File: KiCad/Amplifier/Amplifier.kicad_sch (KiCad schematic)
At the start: 12 parts, among them Q5 NPN, Q6 NPN, U6 TL074

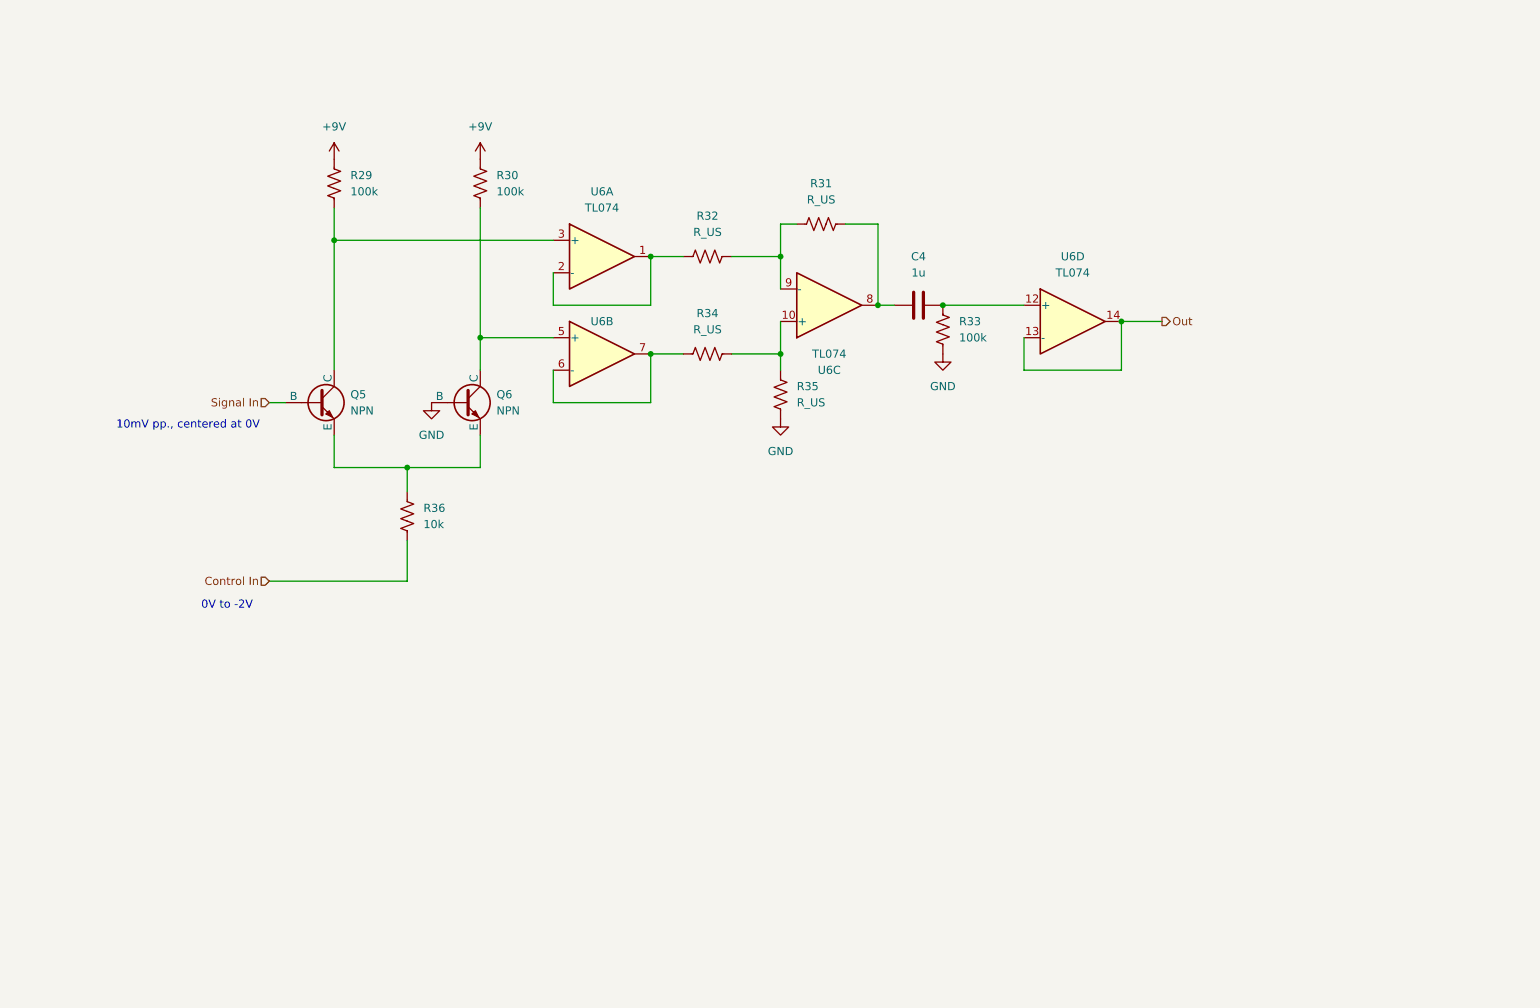
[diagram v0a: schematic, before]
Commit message: started separating into different boards, partially fixed envelope generator
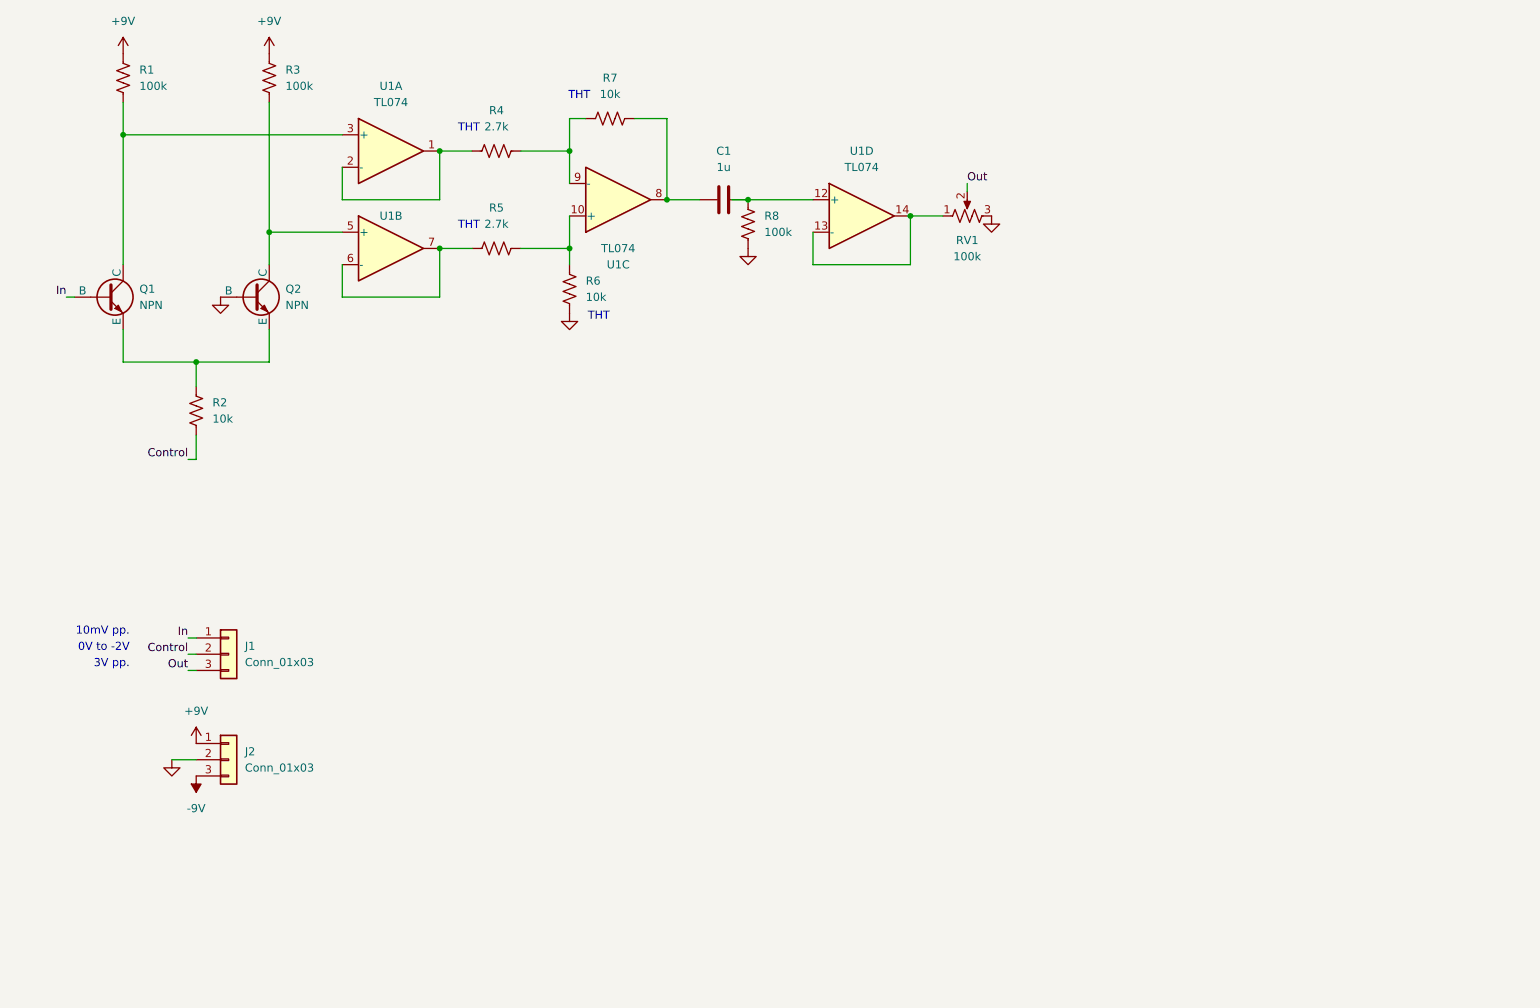
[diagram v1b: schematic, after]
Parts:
- added J1, J2: Conn_01x03, symbol Connector_Generic:Conn_01x03
- added RV1: 100k, symbol Device:R_Potentiometer_US
- R4: renamed from R32; value R_US -> 2.7k
- R5: renamed from R34; value R_US -> 2.7k
- R6: renamed from R35; value R_US -> 10k
- R7: renamed from R31; value R_US -> 10k
- renumbered C4 to C1, Q5 to Q1, Q6 to Q2, R29 to R1, R36 to R2, R30 to R3, R33 to R8, U6 to U1
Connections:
- net +9V: now also J2.1 (Pin_1)
- net GND: now also J2.2 (Pin_2), RV1.3
- net Out: now also J1.3 (Pin_3), RV1.2; no longer U1.13 (-), U1.14
- net Control In renamed Control
- net Control: now also J1.2 (Pin_2)
- net Signal In renamed In
- net In: now also J1.1 (Pin_1)
- new net: RV1.1, U1.13 (-), U1.14
- new net -9V: J2.3 (Pin_3)
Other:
- note added: "10mV pp."
- note added: "3V pp."
- note added: "THT"
- note removed: "10mV pp., centered at 0V"
- moved on the sheet: C1, Q1, Q2, R1, R2, R3, R4, R5, R6, R7, R8, U1A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

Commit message: fixed power board, replaced sketchy voltage divider - op amp cct. with an LDO to product +5V
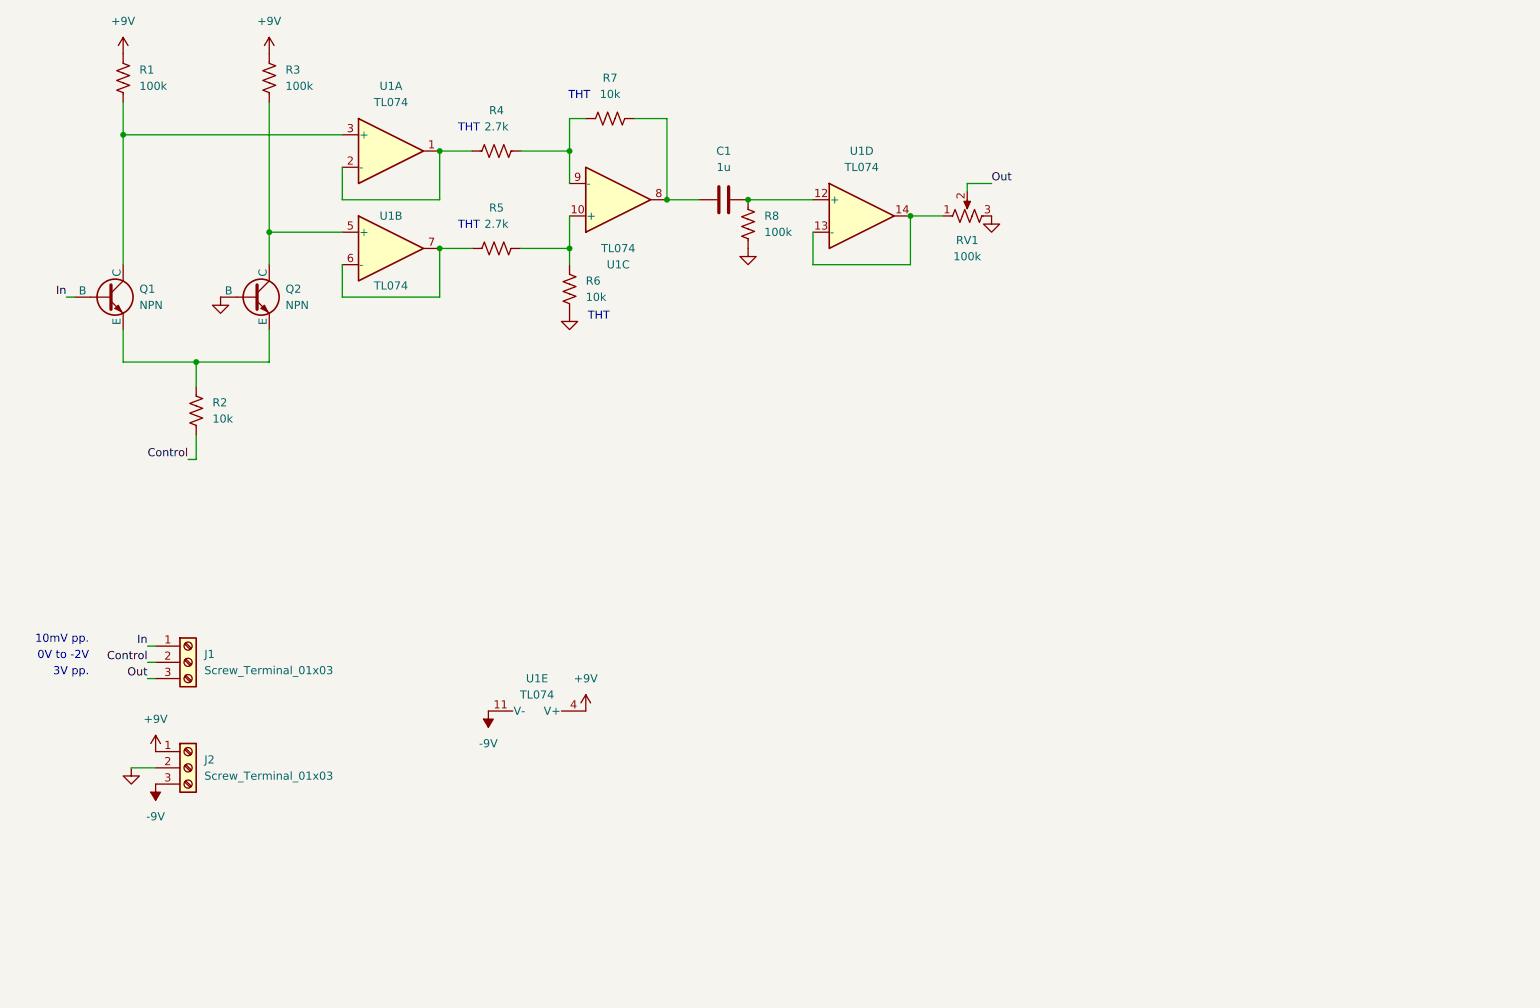
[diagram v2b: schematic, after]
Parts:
- removed J1, J2: Conn_01x03, symbol Connector_Generic:Conn_01x03
- added J1, J2: Screw_Terminal_01x03, symbol Connector:Screw_Terminal_01x03
- added unit 5 of U1
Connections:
- net +9V: now also J2.1 (Pin_1), U1.4 (V+)
- net -9V: now also J2.3 (Pin_3), U1.11 (V-)
- net Control: now also J1.2 (Pin_2)
- net GND: now also J2.2 (Pin_2)
- net In: now also J1.1 (Pin_1)
- net Out: now also J1.3 (Pin_3)

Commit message: finished separating into separate kicad projects
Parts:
- added C? (x2): 0.1u, symbol Device:C_Small
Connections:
- net +9V: now also C?.2
- net -9V: now also C?.1
- net GND: now also C?.1, C?.2
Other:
- moved on the sheet: U1E

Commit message: made oscillator more adjustable
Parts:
- gave numbers to parts that had none: 2
- renumbered C1 to C2
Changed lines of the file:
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@@
 		(dnp no)
 		(fields_autoplaced yes)
-		(property "Reference" "#PWR011"
+		(property "Reference" "#PWR08"
 			(at 99.06 129.54 0)
 			(hide yes)
@@
 			(project "Amplifier"
 				(path "/4b9119d6-fa5d-4921-8a56-e3e986a94725"
-					(reference "#PWR011")
+					(reference "#PWR08")
 					(unit 1)
 				)
@@
 		(dnp no)
 		(fields_autoplaced yes)
-		(property "Reference" "#PWR09"
+		(property "Reference" "#PWR013"
 			(at 166.37 60.96 0)
 			(hide yes)
@@
 			(project "Amplifier"
 				(path "/4b9119d6-fa5d-4921-8a56-e3e986a94725"
-					(reference "#PWR09")
+					(reference "#PWR013")
 					(unit 1)
 				)
@@
 		(dnp no)
 		(fields_autoplaced yes)
-		(property "Reference" "#PWR08"
+		(property "Reference" "#PWR011"
 			(at 128.27 66.04 0)
 			(hide yes)
@@
 			(project "Amplifier"
 				(path "/4b9119d6-fa5d-4921-8a56-e3e986a94725"
-					(reference "#PWR08")
+					(reference "#PWR011")
 					(unit 1)
 				)
@@
 		(dnp no)
 		(fields_autoplaced yes)
-		(property "Reference" "C1"
+		(property "Reference" "C2"
 			(at 124.46 44.45 90)
 			(show_name no)
@@
 			(project "Amplifier"
 				(path "/4b9119d6-fa5d-4921-8a56-e3e986a94725"
-					(reference "C1")
+					(reference "C2")
 					(unit 1)
 				)
@@
 		(dnp no)
 		(fields_autoplaced yes)
-		(property "Reference" "#PWR013"
+		(property "Reference" "#PWR012"
 			(at 129.54 139.7 0)
 			(hide yes)
@@
 			(project "Amplifier"
 				(path "/4b9119d6-fa5d-4921-8a56-e3e986a94725"
-					(reference "#PWR013")
+					(reference "#PWR012")
 					(unit 1)
 				)
@@
 		(dnp no)
 		(fields_autoplaced yes)
-		(property "Reference" "#PWR07"
+		(property "Reference" "#PWR09"
 			(at 100.33 76.2 0)
 			(hide yes)
@@
 			(project "Amplifier"
 				(path "/4b9119d6-fa5d-4921-8a56-e3e986a94725"
-					(reference "#PWR07")
+					(reference "#PWR09")
 					(unit 1)
 				)
@@
 		(dnp no)
 		(fields_autoplaced yes)
-		(property "Reference" "#PWR012"
+		(property "Reference" "#PWR07"
 			(at 88.9 139.7 0)
 			(hide yes)
@@
 			(project "Amplifier"
 				(path "/4b9119d6-fa5d-4921-8a56-e3e986a94725"
-					(reference "#PWR012")
+					(reference "#PWR07")
 					(unit 1)
 				)
@@
 		(dnp no)
 		(fields_autoplaced yes)
-		(property "Reference" "C?"
+		(property "Reference" "C3"
 			(at 124.4536 127 90)
 			(show_name no)
@@
 			(project "Amplifier"
 				(path "/4b9119d6-fa5d-4921-8a56-e3e986a94725"
-					(reference "C?")
+					(reference "C3")
 					(unit 1)
 				)
@@
 		(dnp no)
 		(fields_autoplaced yes)
-		(property "Reference" "C?"
+		(property "Reference" "C1"
 			(at 93.9736 127 90)
 			(show_name no)
@@
 			(project "Amplifier"
 				(path "/4b9119d6-fa5d-4921-8a56-e3e986a94725"
-					(reference "C?")
-					(unit 1)
-				)
+					(reference "C1")
+					(unit 1)
+				)

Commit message: added test points
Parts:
- added TP? (x4): TestPoint_Small, symbol Connector:TestPoint_Small
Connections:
- net Control: now also TP?.1
- net GND: now also TP?.1
- net In: now also TP?.1
- net Out: now also TP?.1

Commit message: added power indicator LEDs
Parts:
- added D1, D2: LED, symbol Device:LED
- added R7, R8: R_US, symbol Device:R_US
- gave numbers to parts that had none: 4
- renumbered R8 to R10, R7 to R9
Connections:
- net +9V: now also D1.2 (A)
- net -9V: now also R8.2
- net GND: now also D2.2 (A), R7.2
- new net: D1.1 (K), R7.1
- new net: D2.1 (K), R8.1

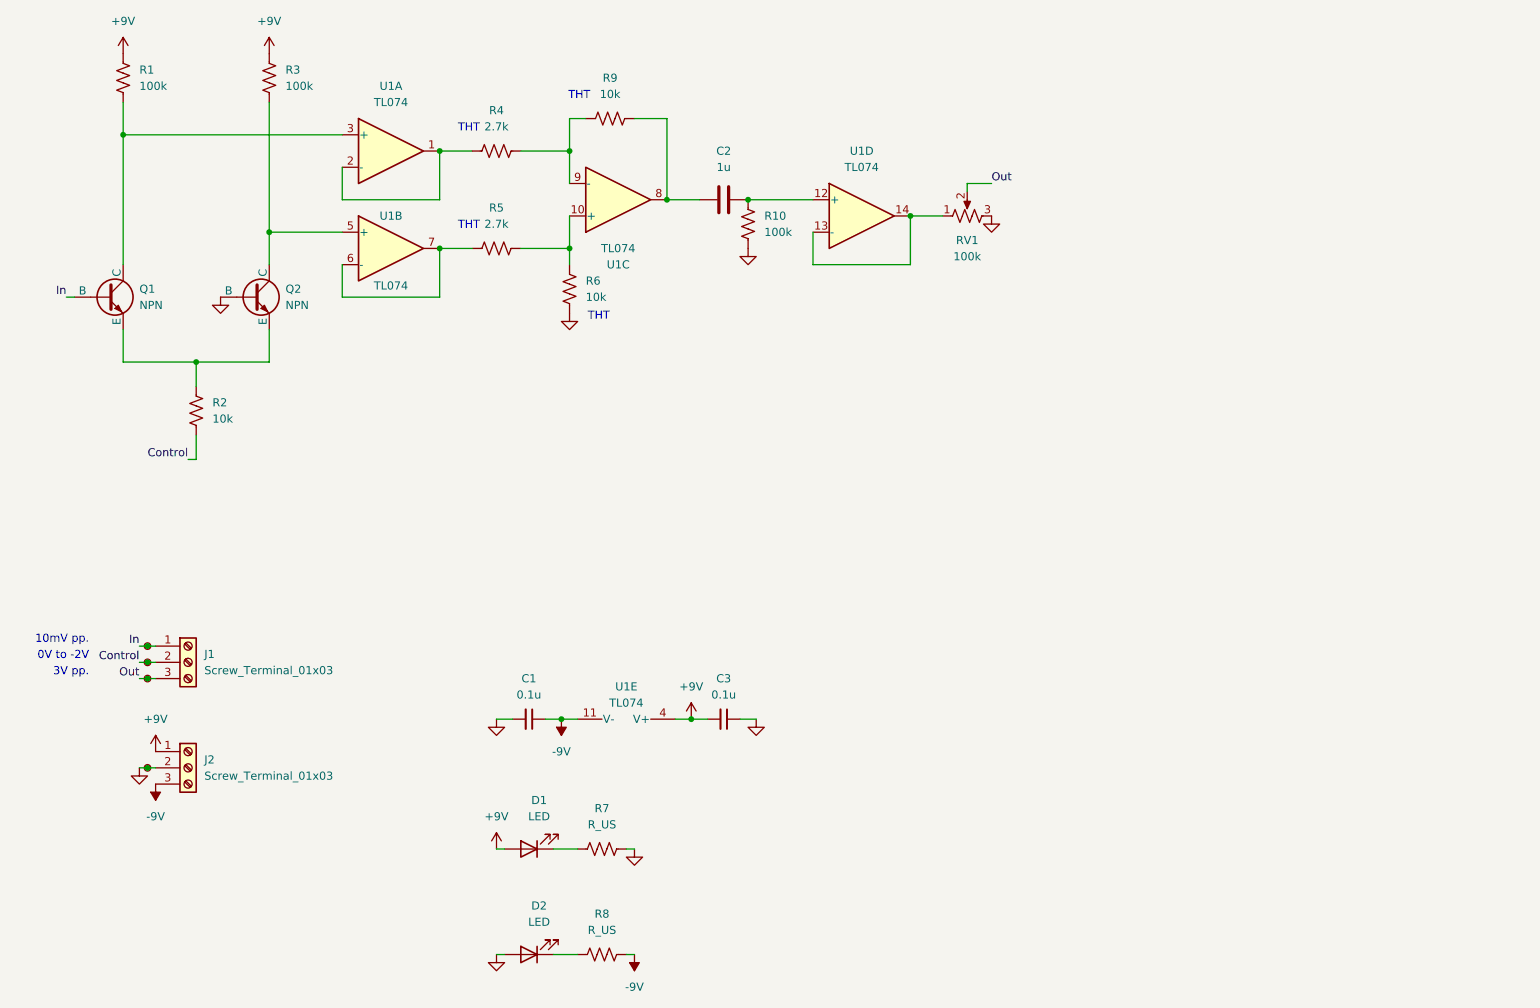
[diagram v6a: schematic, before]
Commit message: amplifier pcb layout done
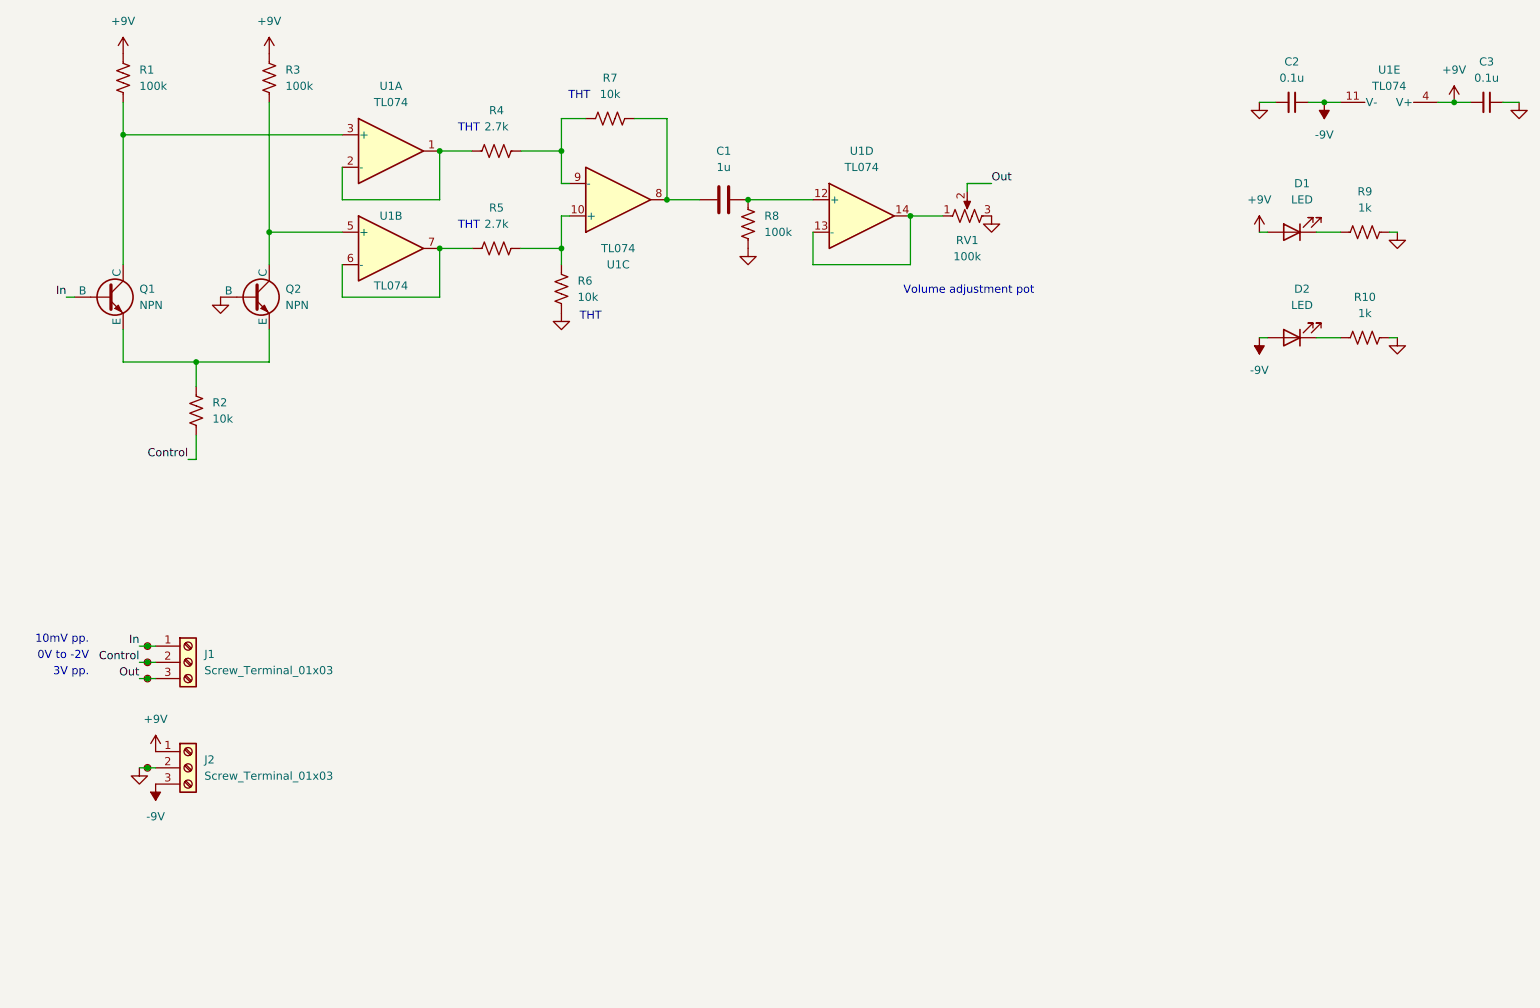
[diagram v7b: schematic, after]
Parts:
- C2: renamed from C1; footprint (none) -> Capacitor_SMD:C_0805_2012Metric
- C3: footprint (none) -> Capacitor_SMD:C_0805_2012Metric
- D1, D2: footprint (none) -> LED_THT:LED_D5.0mm
- J1, J2: footprint (none) -> Header 691137710003:691137710003
- R1, R2, R3: footprint Resistor_SMD:R_0603_1608Metric -> Resistor_SMD:R_0805_2012Metric
- R10: renamed from R8; value R_US -> 1k; footprint (none) -> Resistor_THT:R_Axial_DIN0207_L6.3mm_D2.5mm_P7.62mm_Horizontal
- R8: renamed from R10; footprint Resistor_SMD:R_0603_1608Metric -> Resistor_SMD:R_0805_2012Metric
- R9: renamed from R7; value R_US -> 1k; footprint (none) -> Resistor_THT:R_Axial_DIN0207_L6.3mm_D2.5mm_P7.62mm_Horizontal
- RV1: footprint (none) -> Potentiometer_THT:Potentiometer_Bourns_PTV09A-2_Single_Horizontal
- TP1, TP2, TP3, TP4: footprint (none) -> TestPoint:TestPoint_Keystone_5000-5004_Miniature
- U1: footprint (none) -> Package_DIP:DIP-14_W7.62mm
- renumbered C2 to C1, R9 to R7
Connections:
- net -9V: now also D2.2 (A); no longer R10.2
- net GND: now also R10.2; no longer D2.2 (A)
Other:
- note added: "Volume adjustment pot"
- moved on the sheet: C2, C3, D1, D2, R10, R6, R9, U1E

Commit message: removed unnecessary buffer before filter's output
this drops the number of op amps from 5 to 4, allowing us to use 1 IC instead of 2 ICs with 3 unused circuits.
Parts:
- R10, R9: footprint Resistor_THT:R_Axial_DIN0207_L6.3mm_D2.5mm_P7.62mm_Horizontal -> Resistor_SMD:R_0805_2012Metric
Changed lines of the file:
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@@
 			)
 		)
-		(property "Footprint" "Resistor_THT:R_Axial_DIN0207_L6.3mm_D2.5mm_P7.62mm_Horizontal"
+		(property "Footprint" "Resistor_SMD:R_0805_2012Metric"
 			(at 225.044 56.134 90)
 			(hide yes)
@@
 			)
 		)
-		(property "Footprint" "Resistor_THT:R_Axial_DIN0207_L6.3mm_D2.5mm_P7.62mm_Horizontal"
+		(property "Footprint" "Resistor_SMD:R_0805_2012Metric"
 			(at 225.044 72.644 90)
 			(hide yes)
